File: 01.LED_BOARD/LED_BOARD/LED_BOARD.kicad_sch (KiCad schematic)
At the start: 0 parts

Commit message: LED BOARD - EESCHEMA - SYMBOL
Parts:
- added BT1: Battery_Cell, symbol Device:Battery_Cell
- added D1: LED, symbol Device:LED
- added R1: R, symbol Device:R
- added SW1: SW_DPDT_x2, symbol Switch:SW_DPDT_x2

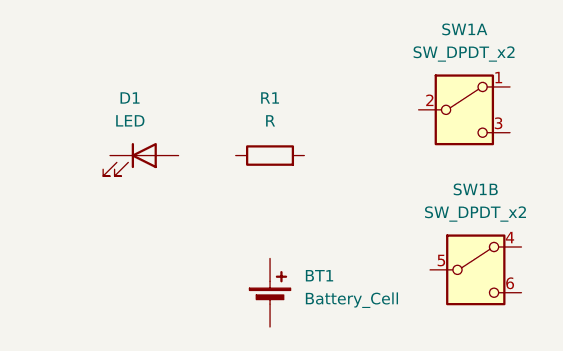
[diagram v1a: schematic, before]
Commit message: LED BOARD - EESCHEMA - ARRANGE, ANNOTATE, ASSOCIATE (FOOTPRINT)
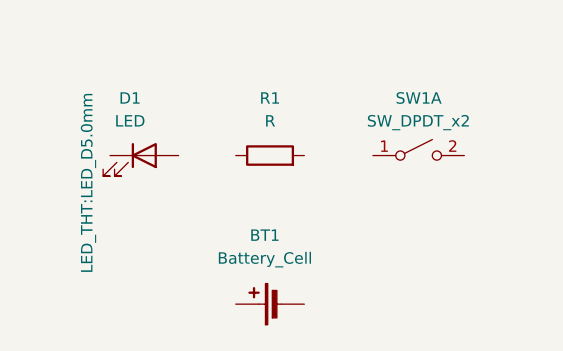
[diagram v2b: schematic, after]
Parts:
- removed unit 2 of SW1
- BT1: footprint (none) -> Battery:BatteryHolder_Keystone_1058_1x2032
- D1: footprint (none) -> LED_THT:LED_D5.0mm
- R1: footprint (none) -> Resistor_THT:R_Axial_DIN0204_L3.6mm_D1.6mm_P7.62mm_Horizontal
- SW1: footprint (none) -> Button_Switch_THT:SW_TH_Tactile_Omron_B3F-10xx; symbol Switch:SW_DPDT_x2 -> Switch:SW_DPST_x2
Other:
- moved on the sheet: BT1
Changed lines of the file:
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@@
 		(on_board yes)
 		(dnp no)
-		(fields_autoplaced yes)
 		(property "Reference" "D1"
 			(at 159.7025 78.74 0)
@@
 			)
 		)
-		(property "Footprint" ""
-			(at 161.29 85.09 0)
-			(effects
-				(font
-					(size 1.27 1.27)
-				)
-				(hide yes)
+		(property "Footprint" "LED_THT:LED_D5.0mm"
+			(at 154.94 88.138 90)
+			(effects
+				(font
+					(size 1.27 1.27)
+				)
 			)
 		)
@@
 	(symbol
 		(lib_id "Device:Battery_Cell")
-		(at 175.26 101.6 0)
+		(at 176.53 101.6 90)
 		(unit 1)
 		(exclude_from_sim no)
@@
 		(fields_autoplaced yes)
 		(property "Reference" "BT1"
-			(at 179.07 98.4884 0)
-			(effects
-				(font
-					(size 1.27 1.27)
-				)
-				(justify left)
+			(at 174.6885 93.98 90)
+			(effects
+				(font
+					(size 1.27 1.27)
+				)
 			)
 		)
 		(property "Value" "Battery_Cell"
-			(at 179.07 101.0284 0)
-			(effects
-				(font
-					(size 1.27 1.27)
-				)
-				(justify left)
-			)
-		)
-		(property "Footprint" ""
-			(at 175.26 100.076 90)
+			(at 174.6885 96.52 90)
+			(effects
+				(font
+					(size 1.27 1.27)
+				)
+			)
+		)
+		(property "Footprint" "Battery:BatteryHolder_Keystone_1058_1x2032"
+			(at 175.006 101.6 90)
 			(effects
 				(font
@@
 		)
 		(property "Datasheet" "~"
-			(at 175.26 100.076 90)
+			(at 175.006 101.6 90)
 			(effects
 				(font
@@
 		)
 		(property "Description" "Single-cell battery"
-			(at 175.26 101.6 0)
+			(at 176.53 101.6 0)
 			(effects
 				(font
@@
 	)
 	(symbol
-		(lib_id "Switch:SW_DPDT_x2")
-		(at 198.12 97.79 0)
-		(unit 2)
-		(exclude_from_sim no)
-		(in_bom yes)
-		(on_board yes)
-		(dnp no)
-		(fields_autoplaced yes)
-		(property "Reference" "SW1"
-			(at 198.12 88.9 0)
-			(effects
-				(font
-					(size 1.27 1.27)
-				)
-			)
-		)
-		(property "Value" "SW_DPDT_x2"
-			(at 198.12 91.44 0)
-			(effects
-				(font
-					(size 1.27 1.27)
-				)
-			)
-		)
-		(property "Footprint" ""
-			(at 198.12 97.79 0)
-			(effects
-				(font
-					(size 1.27 1.27)
-				)
-				(hide yes)
-			)
-		)
-		(property "Datasheet" "~"
-			(at 198.12 97.79 0)
-			(effects
-				(font
-					(size 1.27 1.27)
-				)
-				(hide yes)
-			)
-		)
-		(property "Description" "Switch, dual pole double throw, separate symbols"
-			(at 198.12 97.79 0)
-			(effects
-				(font
-					(size 1.27 1.27)
-				)
-				(hide yes)
-			)
-		)
-		(pin "2"
-		)
-		(pin "5"
-		)
-		(pin "3"
-		)
-		(pin "4"
-		)
-		(pin "6"
-		)
-		(pin "1"
-		)
-		(instances
-			(project ""
-				(path "/f495c5f2-f9f5-4d8a-bf7a-2928a00a870b"
-					(reference "SW1")
-					(unit 2)
-				)
-			)
-		)
-	)
-	(symbol
-		(lib_id "Switch:SW_DPDT_x2")
-		(at 196.85 80.01 0)
+		(lib_id "Switch:SW_DPST_x2")
+		(at 191.77 85.09 0)
 		(unit 1)
 		(exclude_from_sim no)
@@
 		(fields_autoplaced yes)
 		(property "Reference" "SW1"
-			(at 196.85 71.12 0)
+			(at 191.77 78.74 0)
 			(effects
 				(font
@@
 		)
 		(property "Value" "SW_DPDT_x2"
-			(at 196.85 73.66 0)
-			(effects
-				(font
-					(size 1.27 1.27)
-				)
-			)
-		)
-		(property "Footprint" ""
-			(at 196.85 80.01 0)
+			(at 191.77 81.28 0)
+			(effects
+				(font
+					(size 1.27 1.27)
+				)
+			)
+		)
+		(property "Footprint" "Button_Switch_THT:SW_TH_Tactile_Omron_B3F-10xx"
+			(at 191.77 85.09 0)
 			(effects
 				(font
@@
 		)
 		(property "Datasheet" "~"
-			(at 196.85 80.01 0)
-			(effects
-				(font
-					(size 1.27 1.27)
-				)
-				(hide yes)
-			)
-		)
-		(property "Description" "Switch, dual pole double throw, separate symbols"
-			(at 196.85 80.01 0)
+			(at 191.77 85.09 0)
+			(effects
+				(font
+					(size 1.27 1.27)
+				)
+				(hide yes)
+			)
+		)
+		(property "Description" "Single Pole Single Throw (SPST) switch, separate symbol"
+			(at 191.77 85.09 0)
 			(effects
 				(font
@@
 		(pin "2"
 		)
-		(pin "5"
-		)
 		(pin "3"
 		)
 		(pin "4"
-		)
-		(pin "6"
 		)
 		(pin "1"
@@
 			)
 		)
-		(property "Footprint" ""
+		(property "Footprint" "Resistor_THT:R_Axial_DIN0204_L3.6mm_D1.6mm_P7.62mm_Horizontal"
 			(at 175.26 86.868 90)
 			(effects

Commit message: LED BOARD - EESCHEMA - WIRING
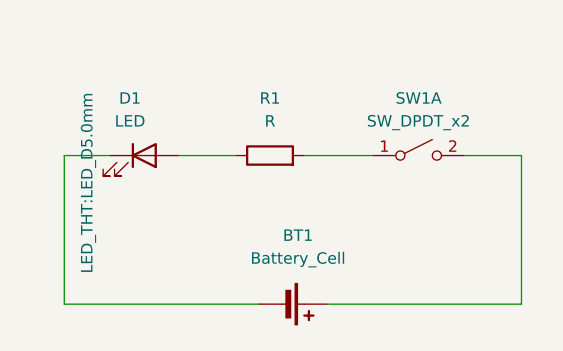
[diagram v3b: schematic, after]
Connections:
- net at D1.1 (K): now also BT1.2 (-)
- net at D1.2 (A): now also R1.1
- net at BT1.1 (+): now also SW1.2 (B)
- net at SW1.1 (A): now also R1.2
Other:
- moved on the sheet: BT1
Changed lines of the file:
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@@
 		(company "GOBAL KRISHNAN ")
+	)
+	(wire
+		(pts
+			(xy 181.61 101.6) (xy 203.2 101.6)
+		)
+		(stroke
+			(width 0)
+			(type default)
+		)
+	)
+	(wire
+		(pts
+			(xy 152.4 101.6) (xy 173.99 101.6)
+		)
+		(stroke
+			(width 0)
+			(type default)
+		)
+	)
+	(wire
+		(pts
+			(xy 157.48 85.09) (xy 152.4 85.09)
+		)
+		(stroke
+			(width 0)
+			(type default)
+		)
+	)
+	(wire
+		(pts
+			(xy 171.45 85.09) (xy 165.1 85.09)
+		)
+		(stroke
+			(width 0)
+			(type default)
+		)
+	)
+	(wire
+		(pts
+			(xy 203.2 85.09) (xy 196.85 85.09)
+		)
+		(stroke
+			(width 0)
+			(type default)
+		)
+	)
+	(wire
+		(pts
+			(xy 203.2 101.6) (xy 203.2 85.09)
+		)
+		(stroke
+			(width 0)
+			(type default)
+		)
+	)
+	(wire
+		(pts
+			(xy 186.69 85.09) (xy 179.07 85.09)
+		)
+		(stroke
+			(width 0)
+			(type default)
+		)
+	)
+	(wire
+		(pts
+			(xy 152.4 85.09) (xy 152.4 101.6)
+		)
+		(stroke
+			(width 0)
+			(type default)
+		)
 	)
 	(symbol
@@
 	(symbol
 		(lib_id "Device:Battery_Cell")
-		(at 176.53 101.6 90)
+		(at 176.53 101.6 270)
 		(unit 1)
 		(exclude_from_sim no)
@@
 		(fields_autoplaced yes)
 		(property "Reference" "BT1"
-			(at 174.6885 93.98 90)
+			(at 178.3715 93.98 90)
 			(effects
 				(font
@@
 		)
 		(property "Value" "Battery_Cell"
-			(at 174.6885 96.52 90)
+			(at 178.3715 96.52 90)
 			(effects
 				(font
@@
 		)
 		(property "Footprint" "Battery:BatteryHolder_Keystone_1058_1x2032"
-			(at 175.006 101.6 90)
+			(at 178.054 101.6 90)
 			(effects
 				(font
@@
 		)
 		(property "Datasheet" "~"
-			(at 175.006 101.6 90)
+			(at 178.054 101.6 90)
 			(effects
 				(font

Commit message: LED BOARD - EESCHEMA - COMMENT
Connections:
- net LED_CATHODE: now reaches BT1.2 (-), D1.1 (K)
- net LED_ANODE: now reaches D1.2 (A), R1.1
- net BAT_POS: now reaches BT1.1 (+), SW1.2 (B)
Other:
- note added: "LED BOARD"
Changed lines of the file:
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@@
 		(company "GOBAL KRISHNAN ")
+	)
+	(rectangle
+		(start 147.447 74.295)
+		(end 205.867 104.775)
+		(stroke
+			(width 0)
+			(type default)
+		)
+		(fill
+			(type none)
+		)
+	)
+	(text "LED BOARD\n"
+		(exclude_from_sim no)
+		(at 153.416 76.2 0)
+		(effects
+			(font
+				(size 1.27 1.27)
+			)
+		)
 	)
 	(wire
@@
 		)
 	)
+	(label "BAT_POS"
+		(at 184.15 101.6 0)
+		(effects
+			(font
+				(size 0.508 0.508)
+			)
+			(justify left bottom)
+		)
+	)
+	(label "LED_ANODE"
+		(at 167.64 85.09 0)
+		(effects
+			(font
+				(size 0.508 0.508)
+			)
+			(justify left bottom)
+		)
+	)
+	(label "LED_CATHODE"
+		(at 152.4 85.09 0)
+		(effects
+			(font
+				(size 0.508 0.508)
+			)
+			(justify left bottom)
+		)
+	)
 	(symbol
 		(lib_id "Device:LED")
@@
 		)
 		(property "Footprint" "LED_THT:LED_D5.0mm"
-			(at 154.94 88.138 90)
+			(at 163.576 87.122 0)
 			(effects
 				(font
-					(size 1.27 1.27)
+					(size 0.508 0.508)
 				)
 			)

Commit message: LED BOARD
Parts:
- SW1: value SW_DPDT_x2 -> SW_DPST_x2
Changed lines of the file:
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@@
 			)
 		)
-		(property "Value" "SW_DPDT_x2"
+		(property "Value" "SW_DPST_x2"
 			(at 191.77 81.28 0)
 			(effects
